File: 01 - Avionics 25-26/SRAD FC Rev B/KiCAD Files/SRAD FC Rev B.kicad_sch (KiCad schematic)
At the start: 0 parts

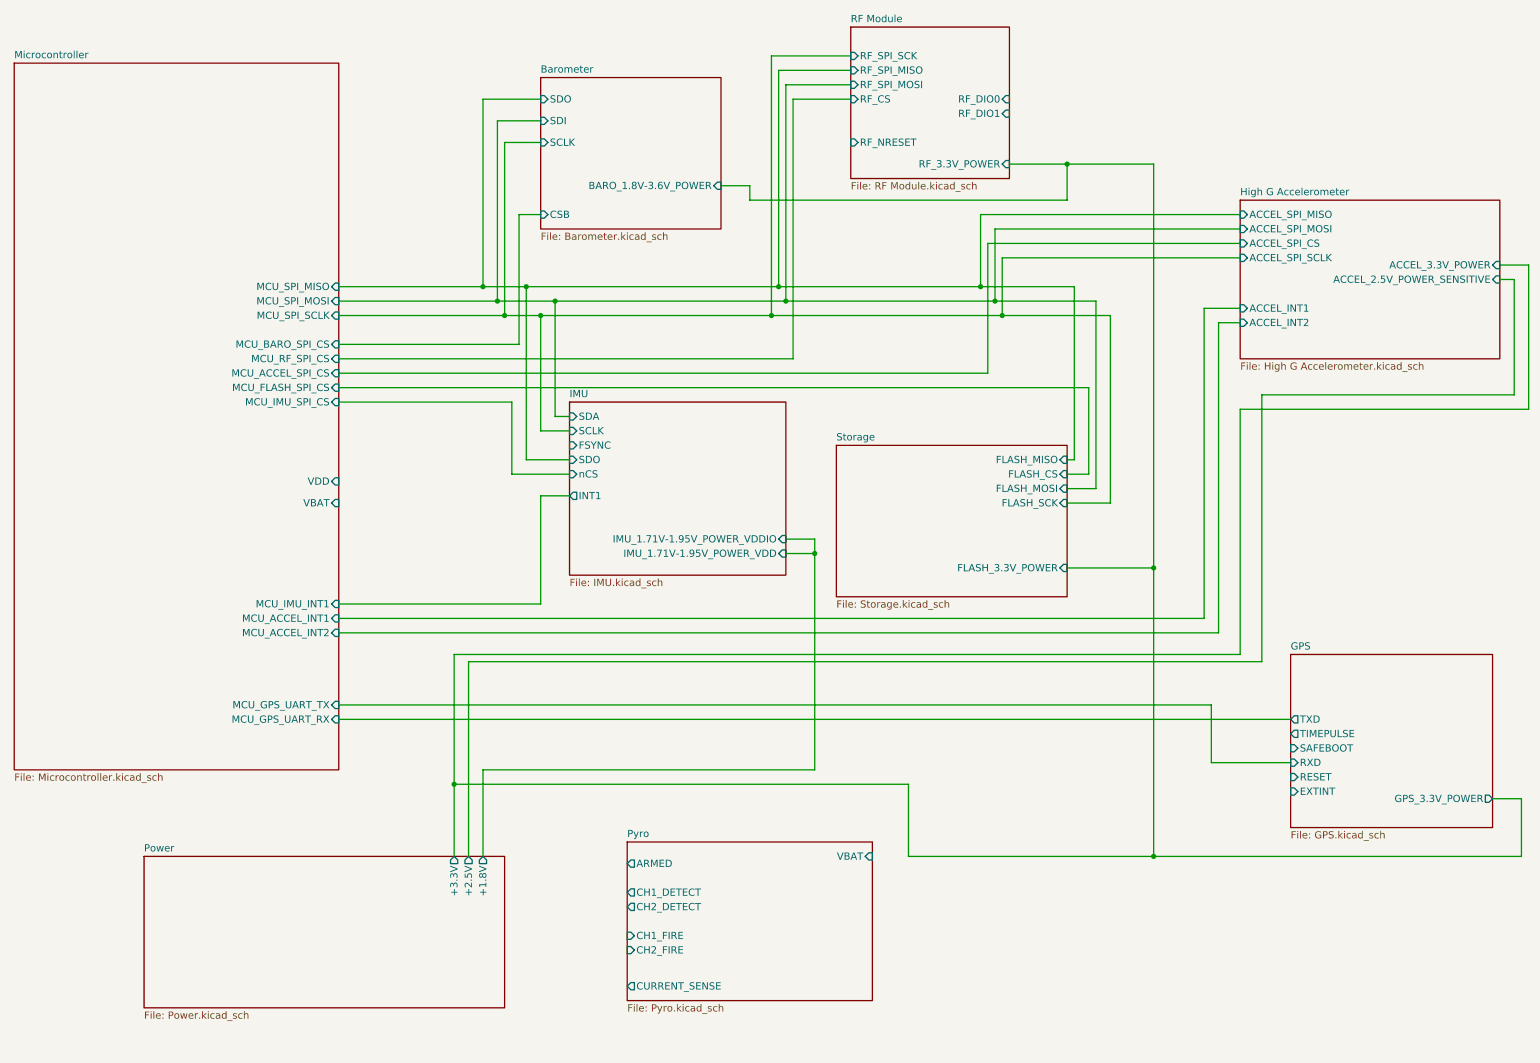
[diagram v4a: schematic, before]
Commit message: wired pyro to the mcu in top level sheet
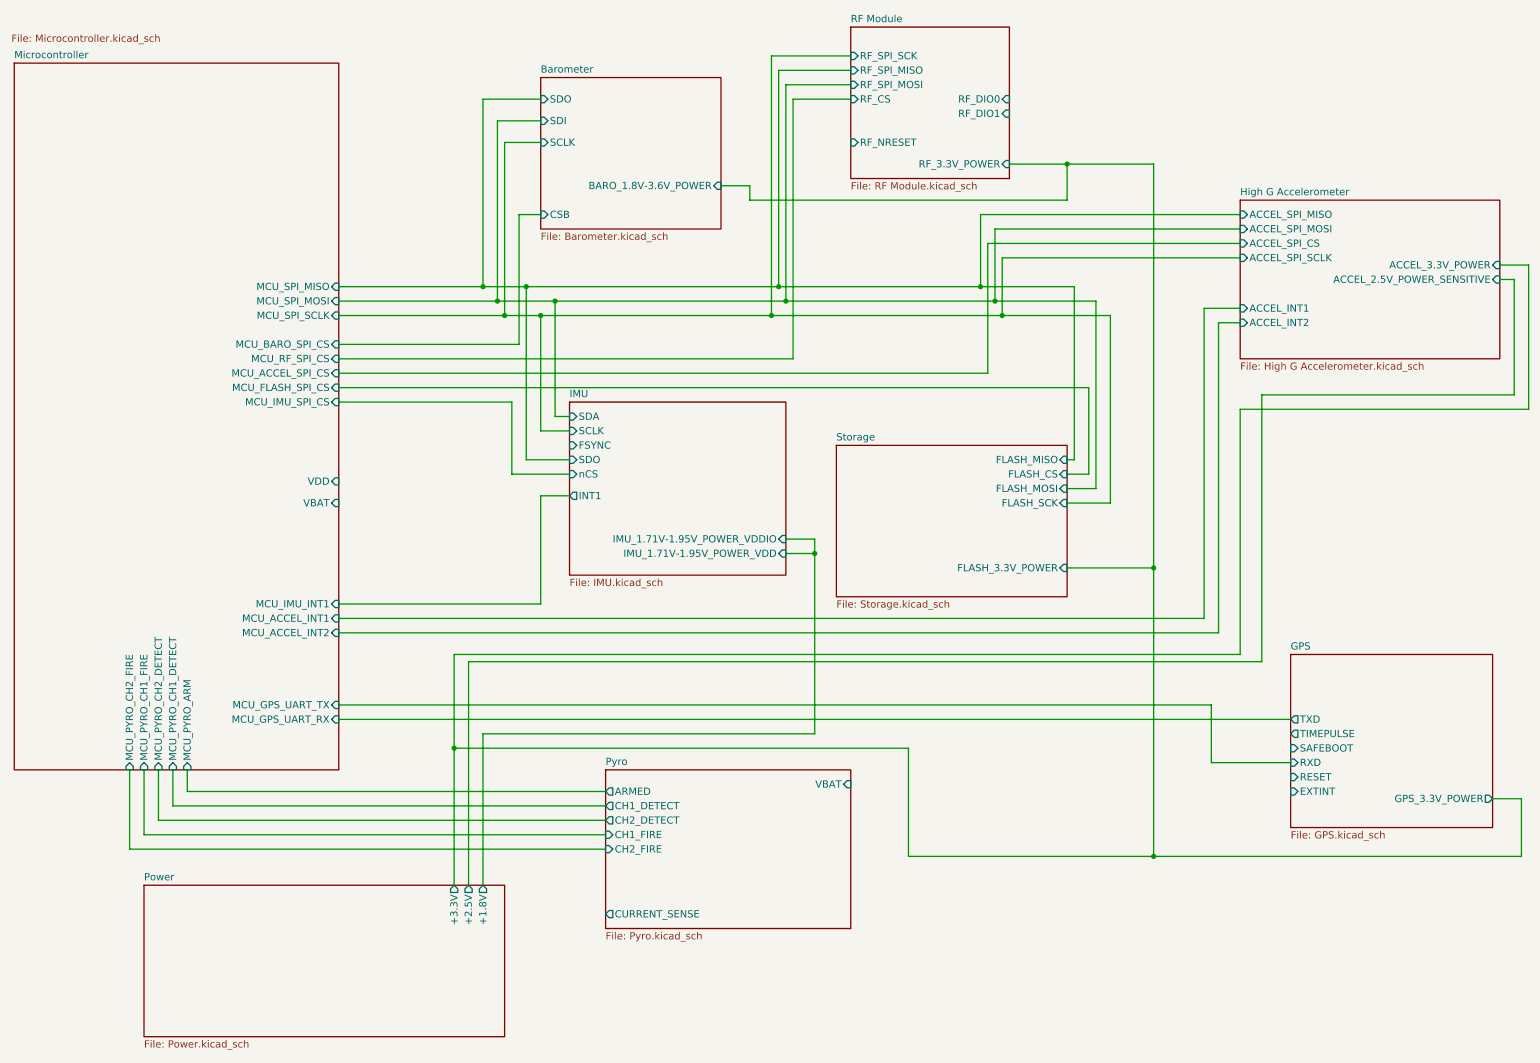
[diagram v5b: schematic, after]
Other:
- sheet Microcontroller ports: added MCU_PYRO_ARM, MCU_PYRO_CH1_DETECT, MCU_PYRO_CH1_FIRE, MCU_PYRO_CH2_DETECT, MCU_PYRO_CH2_FIRE; removed none
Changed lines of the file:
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@@
+	)
+	(junction
+		(at 91.44 143.51)
+		(diameter 0)
+		(color 0 0 0 0)
 	)
 	(junction
@@
 	)
 	(junction
-		(at 91.44 149.86)
-		(diameter 0)
-		(color 0 0 0 0)
-	)
-	(junction
 		(at 99.06 64.77)
 		(diameter 0)
@@
 	(wire
 		(pts
-			(xy 154.94 147.32) (xy 154.94 109.22)
+			(xy 154.94 140.97) (xy 154.94 109.22)
 		)
 		(stroke
@@
 	(wire
 		(pts
-			(xy 93.98 162.56) (xy 93.98 128.27)
+			(xy 44.45 151.13) (xy 118.11 151.13)
+		)
+		(stroke
+			(width 0)
+			(type default)
+		)
+	)
+	(wire
+		(pts
+			(xy 93.98 167.64) (xy 93.98 128.27)
 		)
 		(stroke
@@
 	(wire
 		(pts
-			(xy 96.52 147.32) (xy 154.94 147.32)
+			(xy 96.52 140.97) (xy 154.94 140.97)
 		)
 		(stroke
@@
 	(wire
 		(pts
-			(xy 96.52 162.56) (xy 96.52 147.32)
+			(xy 96.52 167.64) (xy 96.52 140.97)
 		)
 		(stroke
@@
 	(wire
 		(pts
+			(xy 36.83 147.32) (xy 36.83 158.75)
+		)
+		(stroke
+			(width 0)
+			(type default)
+		)
+	)
+	(wire
+		(pts
 			(xy 184.15 49.53) (xy 229.87 49.53)
 		)
@@
 	(wire
 		(pts
-			(xy 171.45 149.86) (xy 91.44 149.86)
+			(xy 171.45 143.51) (xy 91.44 143.51)
+		)
+		(stroke
+			(width 0)
+			(type default)
+		)
+	)
+	(wire
+		(pts
+			(xy 91.44 143.51) (xy 91.44 127)
 		)
 		(stroke
@@
 	(wire
 		(pts
+			(xy 36.83 158.75) (xy 118.11 158.75)
+		)
+		(stroke
+			(width 0)
+			(type default)
+		)
+	)
+	(wire
+		(pts
 			(xy 214.63 40.64) (xy 214.63 111.76)
 		)
@@
 	(wire
 		(pts
+			(xy 39.37 156.21) (xy 118.11 156.21)
+		)
+		(stroke
+			(width 0)
+			(type default)
+		)
+	)
+	(wire
+		(pts
 			(xy 96.52 62.23) (xy 104.14 62.23)
 		)
@@
 	(wire
 		(pts
+			(xy 34.29 161.29) (xy 118.11 161.29)
+		)
+		(stroke
+			(width 0)
+			(type default)
+		)
+	)
+	(wire
+		(pts
 			(xy 99.06 64.77) (xy 109.22 64.77)
 		)
@@
 	(wire
 		(pts
+			(xy 44.45 147.32) (xy 44.45 151.13)
+		)
+		(stroke
+			(width 0)
+			(type default)
+		)
+	)
+	(wire
+		(pts
 			(xy 71.12 67.31) (xy 100.33 67.31)
 		)
@@
 	(wire
 		(pts
-			(xy 91.44 149.86) (xy 91.44 127)
+			(xy 91.44 143.51) (xy 91.44 167.64)
 		)
 		(stroke
@@
 	(wire
 		(pts
+			(xy 41.91 153.67) (xy 118.11 153.67)
+		)
+		(stroke
+			(width 0)
+			(type default)
+		)
+	)
+	(wire
+		(pts
 			(xy 184.15 62.23) (xy 200.66 62.23)
 		)
@@
 	(wire
 		(pts
-			(xy 171.45 162.56) (xy 171.45 149.86)
+			(xy 171.45 162.56) (xy 171.45 143.51)
 		)
 		(stroke
@@
 	(wire
 		(pts
+			(xy 34.29 147.32) (xy 34.29 161.29)
+		)
+		(stroke
+			(width 0)
+			(type default)
+		)
+	)
+	(wire
+		(pts
 			(xy 101.6 95.25) (xy 111.76 95.25)
 		)
@@
 	(wire
 		(pts
+			(xy 39.37 147.32) (xy 39.37 156.21)
+		)
+		(stroke
+			(width 0)
+			(type default)
+		)
+	)
+	(wire
+		(pts
 			(xy 229.87 127) (xy 229.87 83.82)
 		)
@@
 	(wire
 		(pts
-			(xy 91.44 162.56) (xy 91.44 149.86)
-		)
-		(stroke
-			(width 0)
-			(type default)
-		)
-	)
-	(wire
-		(pts
 			(xy 186.69 52.07) (xy 229.87 52.07)
 		)
@@
 	(wire
 		(pts
+			(xy 41.91 147.32) (xy 41.91 153.67)
+		)
+		(stroke
+			(width 0)
+			(type default)
+		)
+	)
+	(wire
+		(pts
 			(xy 199.39 40.64) (xy 189.23 40.64)
 		)
@@
 	)
 	(sheet
-		(at 36.83 162.56)
+		(at 36.83 167.64)
 		(size 63.5 26.67)
 		(exclude_from_sim no)
@@
 		)
 		(property "Sheetname" "Power"
-			(at 36.83 161.8484 0)
+			(at 36.83 166.9284 0)
 			(effects
 				(font
@@
 		)
 		(property "Sheetfile" "Power.kicad_sch"
-			(at 36.83 189.8146 0)
+			(at 36.83 194.8946 0)
 			(effects
 				(font
@@
 		)
 		(pin "+1.8V" output
-			(at 96.52 162.56 90)
+			(at 96.52 167.64 90)
 			(effects
 				(font
@@
 		)
 		(pin "+2.5V" output
-			(at 93.98 162.56 90)
+			(at 93.98 167.64 90)
 			(effects
 				(font
@@
 		)
 		(pin "+3.3V" output
-			(at 91.44 162.56 90)
+			(at 91.44 167.64 90)
 			(effects
 				(font
@@
 		(on_board yes)
 		(dnp no)
-		(fields_autoplaced yes)
 		(stroke
 			(width 0.1524)
@@
 		)
 		(property "Sheetfile" "Microcontroller.kicad_sch"
-			(at 13.97 147.9046 0)
+			(at 13.462 17.78 0)
 			(effects
 				(font
@@
 				)
 				(justify right)
+			)
+		)
+		(pin "MCU_PYRO_CH2_FIRE" input
+			(at 34.29 147.32 270)
+			(effects
+				(font
+					(size 1.27 1.27)
+				)
+				(justify left)
+			)
+		)
+		(pin "MCU_PYRO_CH2_DETECT" input
+			(at 39.37 147.32 270)
+			(effects
+				(font
+					(size 1.27 1.27)
+				)
+				(justify left)
+			)
+		)
+		(pin "MCU_PYRO_ARM" input
+			(at 44.45 147.32 270)
+			(effects
+				(font
+					(size 1.27 1.27)
+				)
+				(justify left)
+			)
+		)
+		(pin "MCU_PYRO_CH1_FIRE" input
+			(at 36.83 147.32 270)
+			(effects
+				(font
+					(size 1.27 1.27)
+				)
+				(justify left)
+			)
+		)
+		(pin "MCU_PYRO_CH1_DETECT" input
+			(at 41.91 147.32 270)
+			(effects
+				(font
+					(size 1.27 1.27)
+				)
+				(justify left)
 			)
 		)
@@
 	)
 	(sheet
-		(at 121.92 160.02)
+		(at 118.11 147.32)
 		(size 43.18 27.94)
 		(exclude_from_sim no)
@@
 		)
 		(property "Sheetname" "Pyro"
-			(at 121.92 159.3084 0)
+			(at 118.11 146.6084 0)
 			(effects
 				(font
@@
 		)
 		(property "Sheetfile" "Pyro.kicad_sch"
-			(at 121.92 188.5446 0)
+			(at 118.11 175.8446 0)
 			(effects
 				(font
@@
 		)
 		(pin "CURRENT_SENSE" output
-			(at 121.92 185.42 180)
+			(at 118.11 172.72 180)
 			(effects
 				(font
@@
 		)
 		(pin "CH1_DETECT" output
-			(at 121.92 168.91 180)
+			(at 118.11 153.67 180)
 			(effects
 				(font
@@
 		)
 		(pin "CH2_DETECT" output
-			(at 121.92 171.45 180)
+			(at 118.11 156.21 180)
 			(effects
 				(font
@@
 		)
 		(pin "CH1_FIRE" input
-			(at 121.92 176.53 180)
+			(at 118.11 158.75 180)
 			(effects
 				(font
@@
 		)
 		(pin "ARMED" output
-			(at 121.92 163.83 180)
+			(at 118.11 151.13 180)
 			(effects
 				(font
@@
 		)
 		(pin "CH2_FIRE" input
-			(at 121.92 179.07 180)
+			(at 118.11 161.29 180)
 			(effects
 				(font
@@
 		)
 		(pin "VBAT" input
-			(at 165.1 162.56 0)
-			(effects
-				(font
+			(at 161.29 149.86 0)
+			(effects
+				(font
